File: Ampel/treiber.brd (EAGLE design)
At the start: 35.6 x 35.6 mm, 11 parts, among them IC1 MC34063AP

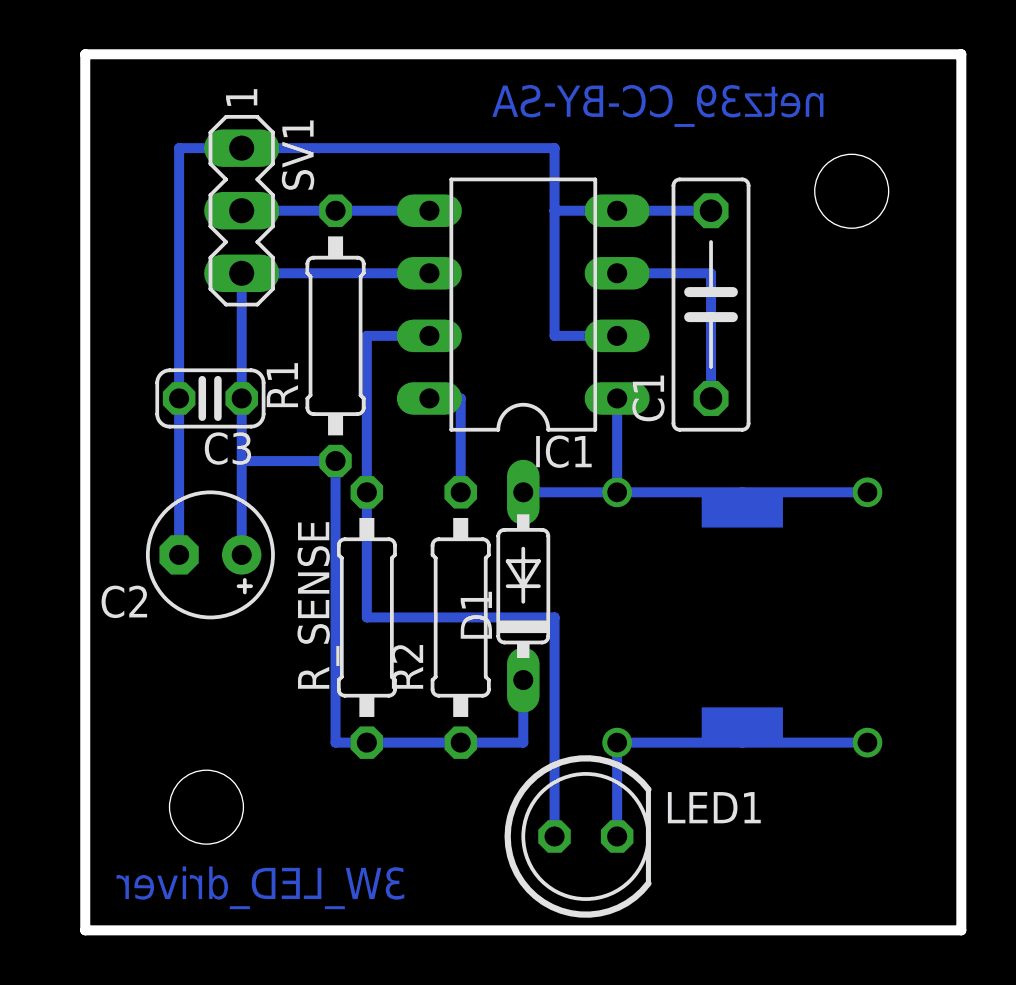
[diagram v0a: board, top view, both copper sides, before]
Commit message: Pad-Größen und Leiterbahnbreiten angepasst
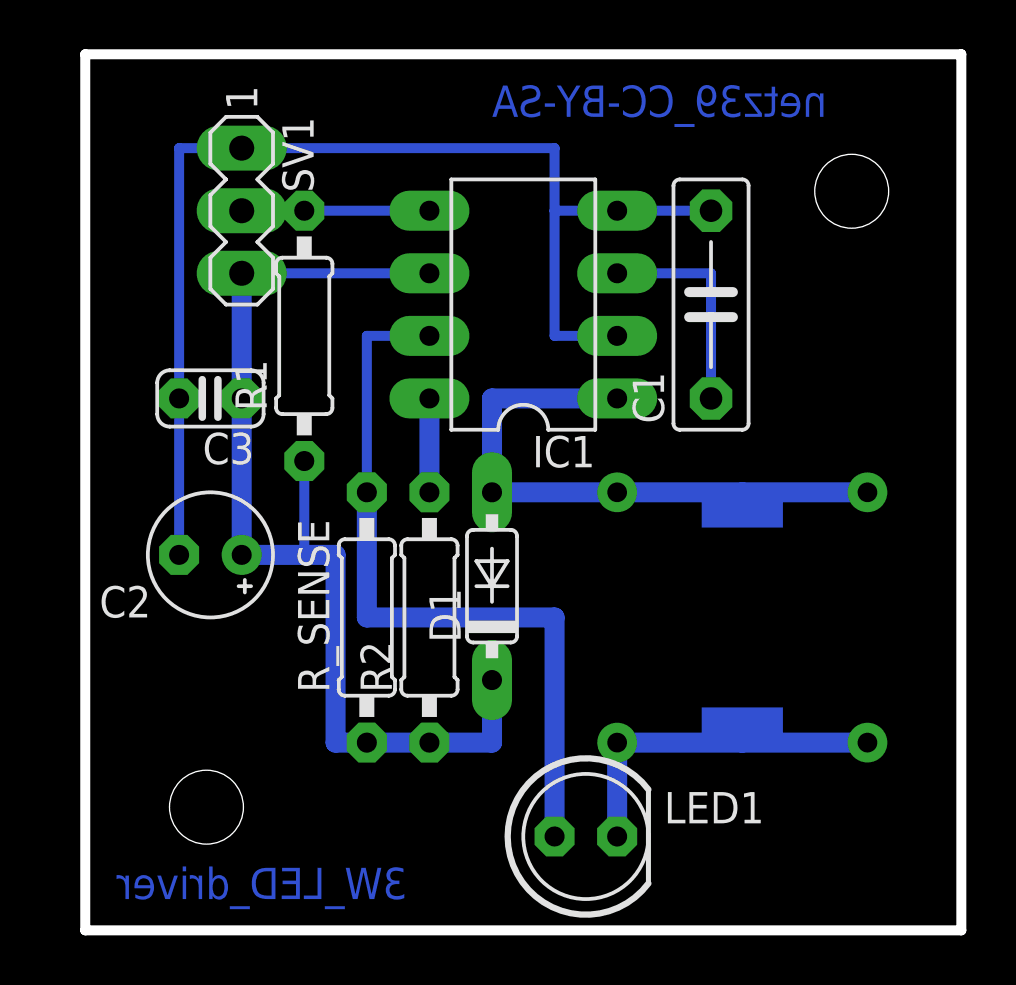
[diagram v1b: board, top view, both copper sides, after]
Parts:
- moved D1 1.27 mm to (16.5, 14.0)
- moved R1 1.27 mm to (8.89, 24.1)
- moved R2 1.27 mm to (14.0, 12.7)
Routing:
- net N$5: track 18.4 -> 24.8 mm
- net VCC: track 44.5 -> 43.2 mm
- net N$2: track 5.08 -> 3.81 mm
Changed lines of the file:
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@@
 <param name="mtCopper" value="0.035mm 0.035mm 0.035mm 0.035mm 0.035mm 0.035mm 0.035mm 0.035mm 0.035mm 0.035mm 0.035mm 0.035mm 0.035mm 0.035mm 0.035mm 0.035mm"/>
 <param name="mtIsolate" value="1.5mm 0.15mm 0.2mm 0.15mm 0.2mm 0.15mm 0.2mm 0.15mm 0.2mm 0.15mm 0.2mm 0.15mm 0.2mm 0.15mm 0.2mm"/>
-<param name="mdWireWire" value="12mil"/>
-<param name="mdWirePad" value="12mil"/>
-<param name="mdWireVia" value="12mil"/>
-<param name="mdPadPad" value="12mil"/>
-<param name="mdPadVia" value="12mil"/>
-<param name="mdViaVia" value="12mil"/>
+<param name="mdWireWire" value="16mil"/>
+<param name="mdWirePad" value="16mil"/>
+<param name="mdWireVia" value="16mil"/>
+<param name="mdPadPad" value="16mil"/>
+<param name="mdPadVia" value="16mil"/>
+<param name="mdViaVia" value="16mil"/>
 <param name="mdSmdPad" value="8mil"/>
 <param name="mdSmdVia" value="8mil"/>
@@
 <param name="mnLayersViaInSmd" value="2"/>
 <param name="mdCopperDimension" value="40mil"/>
-<param name="mdDrill" value="12mil"/>
+<param name="mdDrill" value="16mil"/>
 <param name="mdSmdStop" value="0mil"/>
-<param name="msWidth" value="12mil"/>
+<param name="msWidth" value="16mil"/>
 <param name="msDrill" value="24mil"/>
 <param name="msMicroVia" value="9.99mm"/>
@@
 <param name="rvMicroViaOuter" value="0.25"/>
 <param name="rvMicroViaInner" value="0.25"/>
-<param name="rlMinPadTop" value="10mil"/>
+<param name="rlMinPadTop" value="16mil"/>
 <param name="rlMaxPadTop" value="20mil"/>
-<param name="rlMinPadInner" value="10mil"/>
+<param name="rlMinPadInner" value="16mil"/>
 <param name="rlMaxPadInner" value="20mil"/>
-<param name="rlMinPadBottom" value="10mil"/>
+<param name="rlMinPadBottom" value="16mil"/>
 <param name="rlMaxPadBottom" value="20mil"/>
-<param name="rlMinViaOuter" value="8mil"/>
+<param name="rlMinViaOuter" value="16mil"/>
 <param name="rlMaxViaOuter" value="20mil"/>
-<param name="rlMinViaInner" value="8mil"/>
+<param name="rlMinViaInner" value="16mil"/>
 <param name="rlMaxViaInner" value="20mil"/>
 <param name="rlMinMicroViaOuter" value="4mil"/>
@@
 </element>
 <element name="C1" library="resistor" package="C075-032X103" value="330p" x="25.4" y="25.4" rot="R90"/>
-<element name="R1" library="resistor" package="0207/10" value="4.7K" x="10.16" y="24.13" rot="R90"/>
+<element name="R1" library="resistor" package="0207/10" value="4.7K" x="8.89" y="24.13" rot="R90"/>
 <element name="C2" library="resistor" package="E2,5-5" value="68µ" x="5.08" y="15.24" rot="R180"/>
 <element name="C3" library="resistor" package="C025-024X044" value="100n" x="5.08" y="21.59" rot="R180"/>
-<element name="D1" library="diode" package="DO35-7" value="MBRS240" x="17.78" y="13.97" rot="R90"/>
-<element name="R2" library="resistor" package="0207/10" value="47R" x="15.24" y="12.7" rot="R90"/>
+<element name="D1" library="diode" package="DO35-7" value="MBRS240" x="16.51" y="13.97" rot="R90"/>
+<element name="R2" library="resistor" package="0207/10" value="47R" x="13.97" y="12.7" rot="R90"/>
 <element name="R_SENSE" library="resistor" package="0207/10" value="0.22R" x="11.43" y="12.7" rot="R90"/>
 <element name="LED1" library="led" package="LED5MM" value="3W" x="20.32" y="3.81"/>
@@
 <contactref element="IC1" pad="6"/>
 <contactref element="SV1" pad="3"/>
-<wire x1="15.24" y1="7.62" x2="11.43" y2="7.62" width="0.4064" layer="16"/>
-<wire x1="11.43" y1="7.62" x2="10.16" y2="7.62" width="0.4064" layer="16"/>
-<wire x1="10.16" y1="7.62" x2="10.16" y2="19.05" width="0.4064" layer="16"/>
+<wire x1="13.97" y1="7.62" x2="11.43" y2="7.62" width="0.8128" layer="16"/>
+<wire x1="11.43" y1="7.62" x2="10.16" y2="7.62" width="0.8128" layer="16"/>
 <wire x1="6.35" y1="26.67" x2="13.97" y2="26.67" width="0.4064" layer="16"/>
-<wire x1="6.35" y1="26.67" x2="6.35" y2="21.59" width="0.4064" layer="16"/>
-<wire x1="6.35" y1="21.59" x2="6.35" y2="19.05" width="0.4064" layer="16"/>
-<wire x1="6.35" y1="19.05" x2="6.35" y2="15.24" width="0.4064" layer="16"/>
-<wire x1="17.78" y1="10.16" x2="17.78" y2="7.62" width="0.4064" layer="16"/>
-<wire x1="17.78" y1="7.62" x2="15.24" y2="7.62" width="0.4064" layer="16"/>
-<wire x1="10.16" y1="19.05" x2="6.35" y2="19.05" width="0.4064" layer="16"/>
+<wire x1="6.35" y1="26.67" x2="6.35" y2="21.59" width="0.8128" layer="16"/>
+<wire x1="6.35" y1="21.59" x2="6.35" y2="15.24" width="0.8128" layer="16"/>
+<wire x1="16.51" y1="10.16" x2="16.51" y2="7.62" width="0.8128" layer="16"/>
+<wire x1="16.51" y1="7.62" x2="13.97" y2="7.62" width="0.8128" layer="16"/>
+<wire x1="10.16" y1="7.62" x2="10.16" y2="15.24" width="0.8128" layer="16"/>
+<wire x1="10.16" y1="15.24" x2="8.89" y2="15.24" width="0.8128" layer="16"/>
+<wire x1="8.89" y1="15.24" x2="6.35" y2="15.24" width="0.8128" layer="16"/>
+<wire x1="8.89" y1="19.05" x2="8.89" y2="15.24" width="0.4064" layer="16"/>
 </signal>
 <signal name="PWM">
 <contactref element="IC1" pad="5"/>
 <contactref element="R1" pad="2"/>
-<wire x1="13.97" y1="29.21" x2="10.16" y2="29.21" width="0.4064" layer="16"/>
+<wire x1="13.97" y1="29.21" x2="8.89" y2="29.21" width="0.4064" layer="16"/>
 <contactref element="SV1" pad="2"/>
-<wire x1="6.35" y1="29.21" x2="10.16" y2="29.21" width="0.4064" layer="16"/>
+<wire x1="6.35" y1="29.21" x2="8.89" y2="29.21" width="0.4064" layer="16"/>
 </signal>
 <signal name="GND">
@@
 <wire x1="3.81" y1="21.59" x2="3.81" y2="31.75" width="0.4064" layer="16"/>
 <wire x1="3.81" y1="31.75" x2="6.35" y2="31.75" width="0.4064" layer="16"/>
-<polygon width="0.4064" layer="16" spacing="0.6096" isolate="1.016" thermals="no">
+<polygon width="0.4064" layer="16" spacing="0.6096" isolate="0.6096" thermals="no">
 <vertex x="0" y="35.56"/>
 <vertex x="0" y="0"/>
@@
 <contactref element="IC1" pad="8"/>
 <contactref element="R2" pad="2"/>
-<wire x1="13.97" y1="21.59" x2="15.24" y2="21.59" width="0.4064" layer="16"/>
-<wire x1="15.24" y1="21.59" x2="15.24" y2="17.78" width="0.4064" layer="16"/>
+<wire x1="13.97" y1="21.59" x2="13.97" y2="17.78" width="0.8128" layer="16"/>
 </signal>
 <signal name="N$3">
 <contactref element="R_SENSE" pad="2"/>
 <contactref element="LED1" pad="A"/>
-<wire x1="11.43" y1="17.78" x2="11.43" y2="12.7" width="0.4064" layer="16"/>
-<wire x1="11.43" y1="12.7" x2="19.05" y2="12.7" width="0.4064" layer="16"/>
-<wire x1="19.05" y1="12.7" x2="19.05" y2="3.81" width="0.4064" layer="16"/>
+<wire x1="11.43" y1="17.78" x2="11.43" y2="12.7" width="0.8128" layer="16"/>
+<wire x1="11.43" y1="12.7" x2="19.05" y2="12.7" width="0.8128" layer="16"/>
+<wire x1="19.05" y1="12.7" x2="19.05" y2="3.81" width="0.8128" layer="16"/>
 <wire x1="11.43" y1="24.13" x2="11.43" y2="17.78" width="0.4064" layer="16"/>
 <contactref element="IC1" pad="7"/>
@@
 <contactref element="LED1" pad="K"/>
 <contactref element="L1" pad="1"/>
-<wire x1="21.59" y1="3.81" x2="21.59" y2="7.62" width="0.4064" layer="16"/>
-<wire x1="21.59" y1="7.62" x2="26.67" y2="7.62" width="0.4064" layer="16"/>
+<wire x1="21.59" y1="3.81" x2="21.59" y2="7.62" width="0.8128" layer="16"/>
+<wire x1="21.59" y1="7.62" x2="26.67" y2="7.62" width="0.8128" layer="16"/>
 <wire x1="26.67" y1="7.62" x2="26.67" y2="8.25" width="0.4064" layer="16"/>
 <via x="31.75" y="7.62" extent="1-16" drill="0.8"/>
-<wire x1="26.67" y1="7.62" x2="31.75" y2="7.62" width="0.4064" layer="16"/>
+<wire x1="26.67" y1="7.62" x2="31.75" y2="7.62" width="0.8128" layer="16"/>
 </signal>
 <signal name="N$5">
@@
 <contactref element="D1" pad="A"/>
 <contactref element="IC1" pad="1"/>
-<wire x1="21.59" y1="21.59" x2="21.59" y2="17.78" width="0.4064" layer="16"/>
-<wire x1="17.78" y1="17.78" x2="21.59" y2="17.78" width="0.4064" layer="16"/>
-<wire x1="21.59" y1="17.78" x2="26.67" y2="17.78" width="0.4064" layer="16"/>
+<wire x1="16.51" y1="17.78" x2="26.67" y2="17.78" width="0.8128" layer="16"/>
 <wire x1="26.67" y1="17.78" x2="26.67" y2="17.15" width="0.4064" layer="16"/>
 <via x="31.75" y="17.78" extent="1-16" drill="0.8"/>
-<wire x1="26.67" y1="17.78" x2="31.75" y2="17.78" width="0.4064" layer="16"/>
+<wire x1="26.67" y1="17.78" x2="31.75" y2="17.78" width="0.8128" layer="16"/>
+<wire x1="21.59" y1="21.59" x2="16.51" y2="21.59" width="0.8128" layer="16"/>
+<wire x1="16.51" y1="21.59" x2="16.51" y2="17.78" width="0.8128" layer="16"/>
 </signal>
 <signal name="N$6">
@@
 </signal>
 </signals>
+<errors>
+</errors>
 </board>
 </drawing>

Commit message: Noch ein wenig Layout-Tuning in der LED-Treiberschaltung
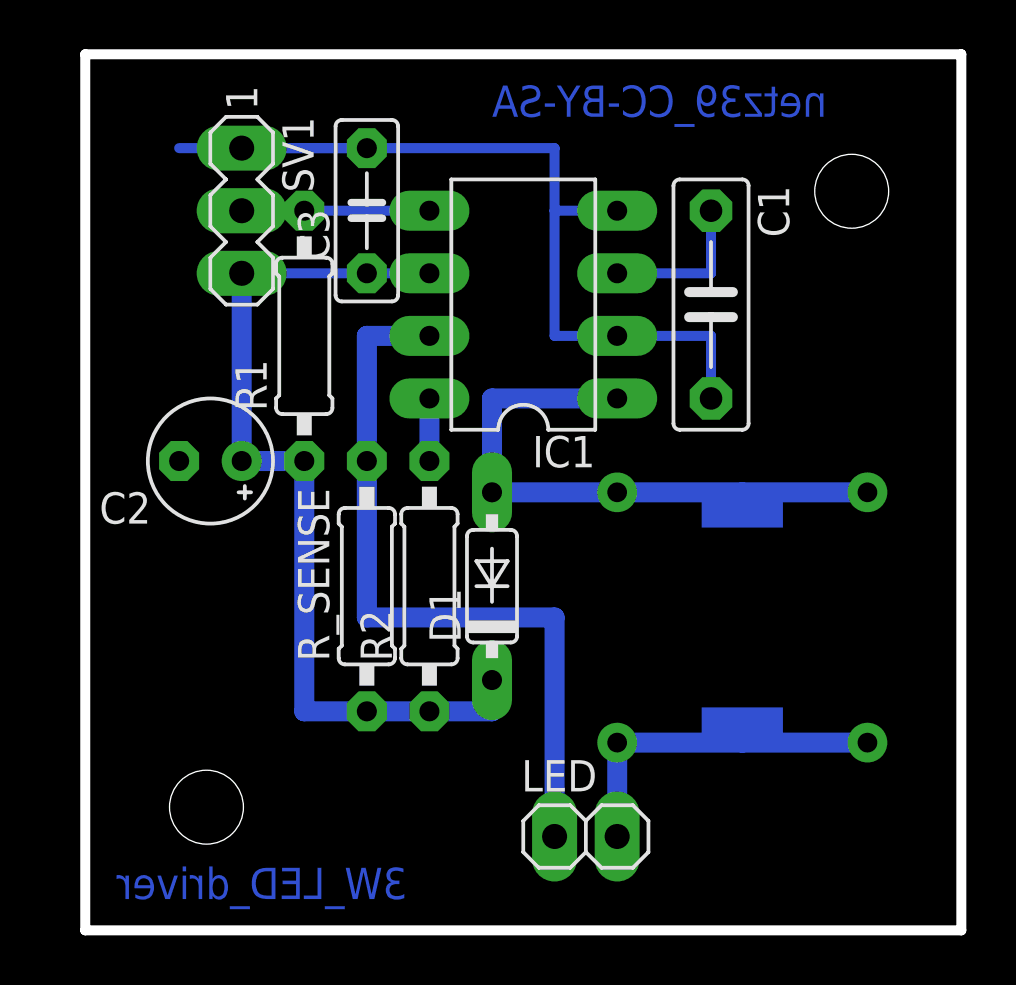
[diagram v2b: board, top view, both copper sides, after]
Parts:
- removed LED1: 3W, led:LED5MM
- added LED: 3W, pinhead:1X02
- C3: device resistor:C025-024X044 -> capacitor-wima:C5B2.5
- moved C3 9.92 mm to (11.4, 29.2), turned to 90 degrees
- moved C2 3.81 mm to (5.08, 19.1)
- moved R2 1.27 mm to (14.0, 14.0)
- moved R_SENSE 1.27 mm to (11.4, 14.0)
- turned C1 to 270 degrees
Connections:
- net N$3: now also LED.1; no longer LED1.A
- net N$4: now also LED.2; no longer LED1.K
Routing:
- net GND: track 48.3 -> 39.4 mm
- net VCC: track 43.2 -> 36.8 mm
- net N$1: track 8.89 -> 6.35 mm
- net N$2: track 3.81 -> 2.54 mm
- net N$4: vias 1 -> 0
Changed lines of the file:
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@@
 <attribute name="OC_FARNELL" value="unknown" x="-26.67" y="11.43" size="1.778" layer="27" rot="R270" display="off"/>
 </element>
-<element name="C1" library="resistor" package="C075-032X103" value="330p" x="25.4" y="25.4" rot="R90"/>
+<element name="C1" library="resistor" package="C075-032X103" value="330p" x="25.4" y="25.4" rot="R270"/>
 <element name="R1" library="resistor" package="0207/10" value="4.7K" x="8.89" y="24.13" rot="R90"/>
-<element name="C2" library="resistor" package="E2,5-5" value="68µ" x="5.08" y="15.24" rot="R180"/>
-<element name="C3" library="resistor" package="C025-024X044" value="100n" x="5.08" y="21.59" rot="R180"/>
+<element name="C2" library="resistor" package="E2,5-5" value="68µ" x="5.08" y="19.05" rot="R180"/>
+<element name="C3" library="capacitor-wima" package="C5B2.5" value="100n" x="11.43" y="29.21" rot="R90"/>
 <element name="D1" library="diode" package="DO35-7" value="MBRS240" x="16.51" y="13.97" rot="R90"/>
-<element name="R2" library="resistor" package="0207/10" value="47R" x="13.97" y="12.7" rot="R90"/>
-<element name="R_SENSE" library="resistor" package="0207/10" value="0.22R" x="11.43" y="12.7" rot="R90"/>
-<element name="LED1" library="led" package="LED5MM" value="3W" x="20.32" y="3.81"/>
+<element name="R2" library="resistor" package="0207/10" value="47R" x="13.97" y="13.97" rot="R90"/>
+<element name="R_SENSE" library="resistor" package="0207/10" value="0.22R" x="11.43" y="13.97" rot="R90"/>
 <element name="L1" library="inductors" package="DR1030" value="220µ" x="26.67" y="12.7" rot="MR180"/>
+<element name="LED" library="pinhead" package="1X02" value="3W" x="20.32" y="3.81"/>
 </elements>
 <signals>
@@
 <contactref element="IC1" pad="6"/>
 <contactref element="SV1" pad="3"/>
-<wire x1="13.97" y1="7.62" x2="11.43" y2="7.62" width="0.8128" layer="16"/>
-<wire x1="11.43" y1="7.62" x2="10.16" y2="7.62" width="0.8128" layer="16"/>
-<wire x1="6.35" y1="26.67" x2="13.97" y2="26.67" width="0.4064" layer="16"/>
-<wire x1="6.35" y1="26.67" x2="6.35" y2="21.59" width="0.8128" layer="16"/>
-<wire x1="6.35" y1="21.59" x2="6.35" y2="15.24" width="0.8128" layer="16"/>
-<wire x1="16.51" y1="10.16" x2="16.51" y2="7.62" width="0.8128" layer="16"/>
-<wire x1="16.51" y1="7.62" x2="13.97" y2="7.62" width="0.8128" layer="16"/>
-<wire x1="10.16" y1="7.62" x2="10.16" y2="15.24" width="0.8128" layer="16"/>
-<wire x1="10.16" y1="15.24" x2="8.89" y2="15.24" width="0.8128" layer="16"/>
-<wire x1="8.89" y1="15.24" x2="6.35" y2="15.24" width="0.8128" layer="16"/>
-<wire x1="8.89" y1="19.05" x2="8.89" y2="15.24" width="0.4064" layer="16"/>
+<wire x1="13.97" y1="8.89" x2="11.43" y2="8.89" width="0.8128" layer="16"/>
+<wire x1="11.43" y1="8.89" x2="8.89" y2="8.89" width="0.8128" layer="16"/>
+<wire x1="11.43" y1="26.67" x2="13.97" y2="26.67" width="0.4064" layer="16"/>
+<wire x1="16.51" y1="10.16" x2="16.51" y2="8.89" width="0.8128" layer="16"/>
+<wire x1="16.51" y1="8.89" x2="13.97" y2="8.89" width="0.8128" layer="16"/>
+<wire x1="8.89" y1="8.89" x2="8.89" y2="19.05" width="0.8128" layer="16"/>
+<wire x1="11.43" y1="26.67" x2="6.35" y2="26.67" width="0.4064" layer="16"/>
+<wire x1="6.35" y1="19.05" x2="6.35" y2="26.67" width="0.8128" layer="16"/>
+<wire x1="6.35" y1="19.05" x2="8.89" y2="19.05" width="0.8128" layer="16"/>
 </signal>
 <signal name="PWM">
@@
 <contactref element="C2" pad="-"/>
 <contactref element="C3" pad="2"/>
-<wire x1="21.59" y1="29.21" x2="25.4" y2="29.21" width="0.4064" layer="16"/>
 <wire x1="21.59" y1="29.21" x2="19.05" y2="29.21" width="0.4064" layer="16"/>
 <wire x1="19.05" y1="29.21" x2="19.05" y2="24.13" width="0.4064" layer="16"/>
@@
 <wire x1="6.35" y1="31.75" x2="19.05" y2="31.75" width="0.4064" layer="16"/>
 <wire x1="19.05" y1="31.75" x2="19.05" y2="29.21" width="0.4064" layer="16"/>
-<wire x1="3.81" y1="15.24" x2="3.81" y2="21.59" width="0.4064" layer="16"/>
-<wire x1="3.81" y1="21.59" x2="3.81" y2="31.75" width="0.4064" layer="16"/>
+<wire x1="11.43" y1="31.75" x2="6.35" y2="31.75" width="0.4064" layer="16"/>
 <wire x1="3.81" y1="31.75" x2="6.35" y2="31.75" width="0.4064" layer="16"/>
 <polygon width="0.4064" layer="16" spacing="0.6096" isolate="0.6096" thermals="no">
@@
 <vertex x="35.56" y="35.56"/>
 </polygon>
+<wire x1="25.4" y1="21.59" x2="25.4" y2="24.13" width="0.4064" layer="16"/>
+<wire x1="25.4" y1="24.13" x2="21.59" y2="24.13" width="0.4064" layer="16"/>
 </signal>
 <signal name="N$1">
 <contactref element="IC1" pad="3"/>
 <contactref element="C1" pad="1"/>
-<wire x1="25.4" y1="21.59" x2="25.4" y2="26.67" width="0.4064" layer="16"/>
+<wire x1="25.4" y1="29.21" x2="25.4" y2="26.67" width="0.4064" layer="16"/>
 <wire x1="25.4" y1="26.67" x2="21.59" y2="26.67" width="0.4064" layer="16"/>
 </signal>
@@
 <contactref element="IC1" pad="8"/>
 <contactref element="R2" pad="2"/>
-<wire x1="13.97" y1="21.59" x2="13.97" y2="17.78" width="0.8128" layer="16"/>
+<wire x1="13.97" y1="21.59" x2="13.97" y2="19.05" width="0.8128" layer="16"/>
 </signal>
 <signal name="N$3">
 <contactref element="R_SENSE" pad="2"/>
-<contactref element="LED1" pad="A"/>
-<wire x1="11.43" y1="17.78" x2="11.43" y2="12.7" width="0.8128" layer="16"/>
+<wire x1="11.43" y1="19.05" x2="11.43" y2="12.7" width="0.8128" layer="16"/>
 <wire x1="11.43" y1="12.7" x2="19.05" y2="12.7" width="0.8128" layer="16"/>
-<wire x1="19.05" y1="12.7" x2="19.05" y2="3.81" width="0.8128" layer="16"/>
-<wire x1="11.43" y1="24.13" x2="11.43" y2="17.78" width="0.4064" layer="16"/>
+<wire x1="11.43" y1="24.13" x2="11.43" y2="19.05" width="0.8128" layer="16"/>
 <contactref element="IC1" pad="7"/>
-<wire x1="11.43" y1="24.13" x2="13.97" y2="24.13" width="0.4064" layer="16"/>
-</signal>
-<signal name="N$4">
-<contactref element="LED1" pad="K"/>
-<contactref element="L1" pad="1"/>
-<wire x1="21.59" y1="3.81" x2="21.59" y2="7.62" width="0.8128" layer="16"/>
-<wire x1="21.59" y1="7.62" x2="26.67" y2="7.62" width="0.8128" layer="16"/>
-<wire x1="26.67" y1="7.62" x2="26.67" y2="8.25" width="0.4064" layer="16"/>
-<via x="31.75" y="7.62" extent="1-16" drill="0.8"/>
-<wire x1="26.67" y1="7.62" x2="31.75" y2="7.62" width="0.8128" layer="16"/>
+<wire x1="11.43" y1="24.13" x2="13.97" y2="24.13" width="0.8128" layer="16"/>
+<contactref element="LED" pad="1"/>
+<wire x1="19.05" y1="3.81" x2="19.05" y2="12.7" width="0.8128" layer="16"/>
 </signal>
 <signal name="N$5">
@@
 <signal name="N$15">
 </signal>
+<signal name="N$4">
+<contactref element="L1" pad="1"/>
+<contactref element="LED" pad="2"/>
+<wire x1="21.59" y1="3.81" x2="21.59" y2="7.62" width="0.8128" layer="16"/>
+<wire x1="21.59" y1="7.62" x2="26.67" y2="7.62" width="0.8128" layer="16"/>
+<wire x1="31.75" y1="7.62" x2="26.67" y2="7.62" width="0.8128" layer="16"/>
+<wire x1="26.67" y1="7.62" x2="26.67" y2="8.25" width="0.4064" layer="16"/>
+</signal>
+<signal name="N$11">
+<via x="31.75" y="7.62" extent="1-16" drill="0.8"/>
+</signal>
 </signals>
